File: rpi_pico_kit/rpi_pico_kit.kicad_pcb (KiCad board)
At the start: 2 copper layers, 99.1 x 99.1 mm, 242 parts, among them J1 DC Jack 5.5x2.1mm, J10 OLED Display SSD1306, J11 Conn_01x04_Male, J12 Conn_01x04_Male, J13 AudioJack-CUI-SJ-3523-SMT, J14 AudioJack-CUI-SJ-3523-SMT, J2 USB_B, J3 Conn_01x03_Male, J4 DB15_Female_HighDensity_Mount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, J5 HDMI_A, J6 Conn_01x08_Male, J7 Conn_01x08_Male, J8 Conn_01x08_Male, J9 Micro_SD_Card_Det, Q1 DMN63D8L-7, Q2 DMN63D8L-7, Q3 DMN63D8L-7, Q4 DMN63D8L-7, Q5 DMN63D8L-7, Q6 DMN63D8L-7, Q7 DMN63D8L-7, SW1 SW_Push, SW10 SW_Push, SW2 RotaryEncoder_Switch, SW3 SW_Push, SW4 SW_Push, SW5 SW_Push, SW6 SW_Push, SW7 SW_Push, SW8 SW_Push, SW9 SW_Push, U1 RPi Pico, U10 74LVC2G34GV, U11 PCM5101A, U2 NCP1117-3.3_SOT223, U3 RP2040, U4 W25Q16JVSSIQ, U5 74HC14, U6 74HC14, U7 MCP23S08-xSO, U8 AT24CS32, U9 NCP115-3.3_SOT23-5, Y1 12MHz

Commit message: pcb changes
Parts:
- moved C22 246.1 mm to (174.4, 100.7)
- moved C23 246.1 mm to (160.9, 115.3)
- moved Q3 246.1 mm to (160.9, 111.6)
- moved R25 246.1 mm to (160.7, 122.0)
- moved R26 246.1 mm to (170.6, 113.8)
- moved R27 246.1 mm to (183.9, 103.7)
- moved R28 246.1 mm to (188.7, 100.3)
- moved R29 246.1 mm to (179.1, 106.6)
- moved R32 246.1 mm to (175.4, 112.6)
- moved R35 246.1 mm to (180.1, 109.6)
- moved R36 246.1 mm to (165.4, 121.3)
- moved R37 246.1 mm to (165.6, 118.3)
- moved R38 246.1 mm to (182.8, 97.3)
- moved R41 246.1 mm to (160.8, 118.3)
- moved R42 246.1 mm to (174.3, 106.7)
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
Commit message: pcb changes
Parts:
- moved U7 208.5 mm to (48.6, 185.9)
- moved C1 205.3 mm to (-30.2, 171.8)
- moved C11 205.3 mm to (-25.4, 171.8)
- moved C12 205.3 mm to (-30.2, 174.8)
- moved C14 205.3 mm to (-28.8, 168.8)
- moved C6 205.3 mm to (-23.9, 168.8)
- moved R10 205.3 mm to (-38.5, 186.3)
- moved R12 205.3 mm to (-19.2, 169.1)
- moved R13 205.3 mm to (-19.2, 166.2)
- moved R15 205.3 mm to (-38.5, 189.2)
- moved R17 205.3 mm to (-25.5, 174.7)
- moved R18 205.3 mm to (-29.0, 177.8)
- moved TP4 205.3 mm to (-39.4, 192.2)
- moved C10 205.3 mm to (-38.6, 180.3)
- moved C15 205.3 mm to (-20.4, 163.2)
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
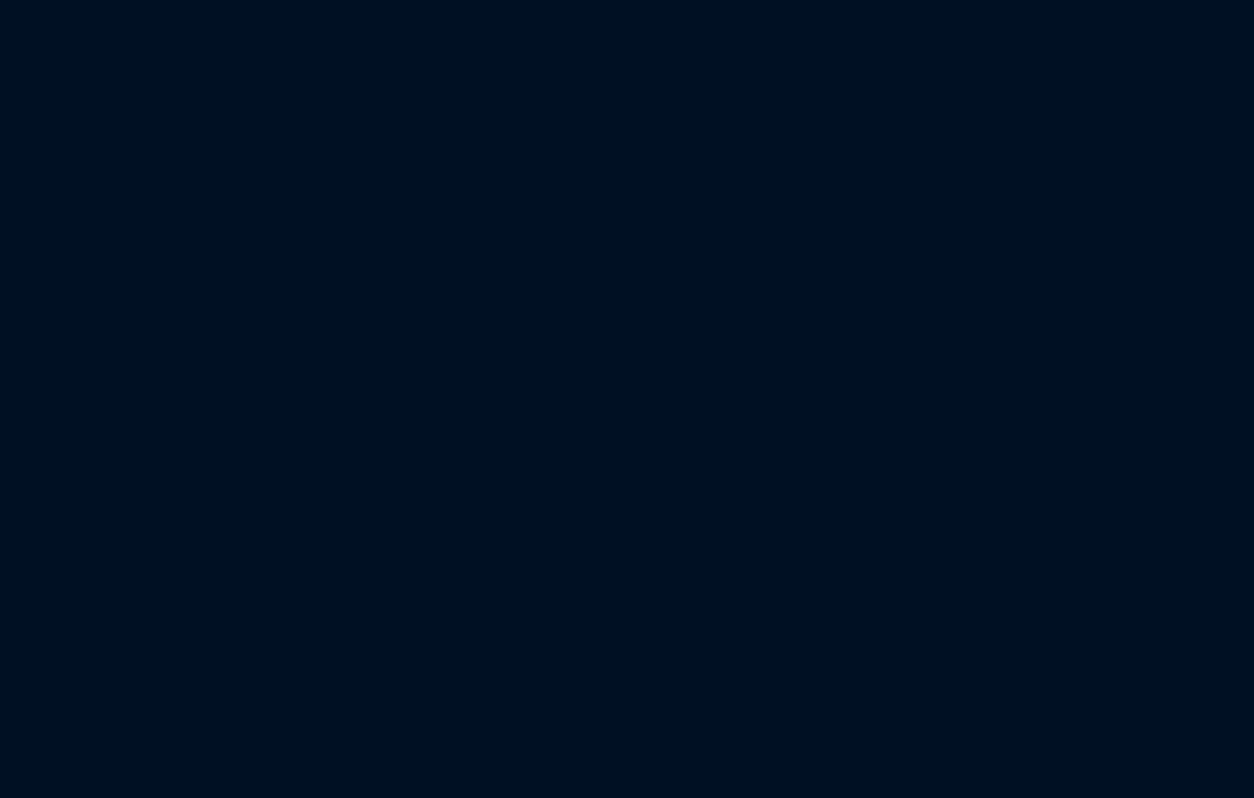
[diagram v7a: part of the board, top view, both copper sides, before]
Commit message: added footprints for resistor arrays
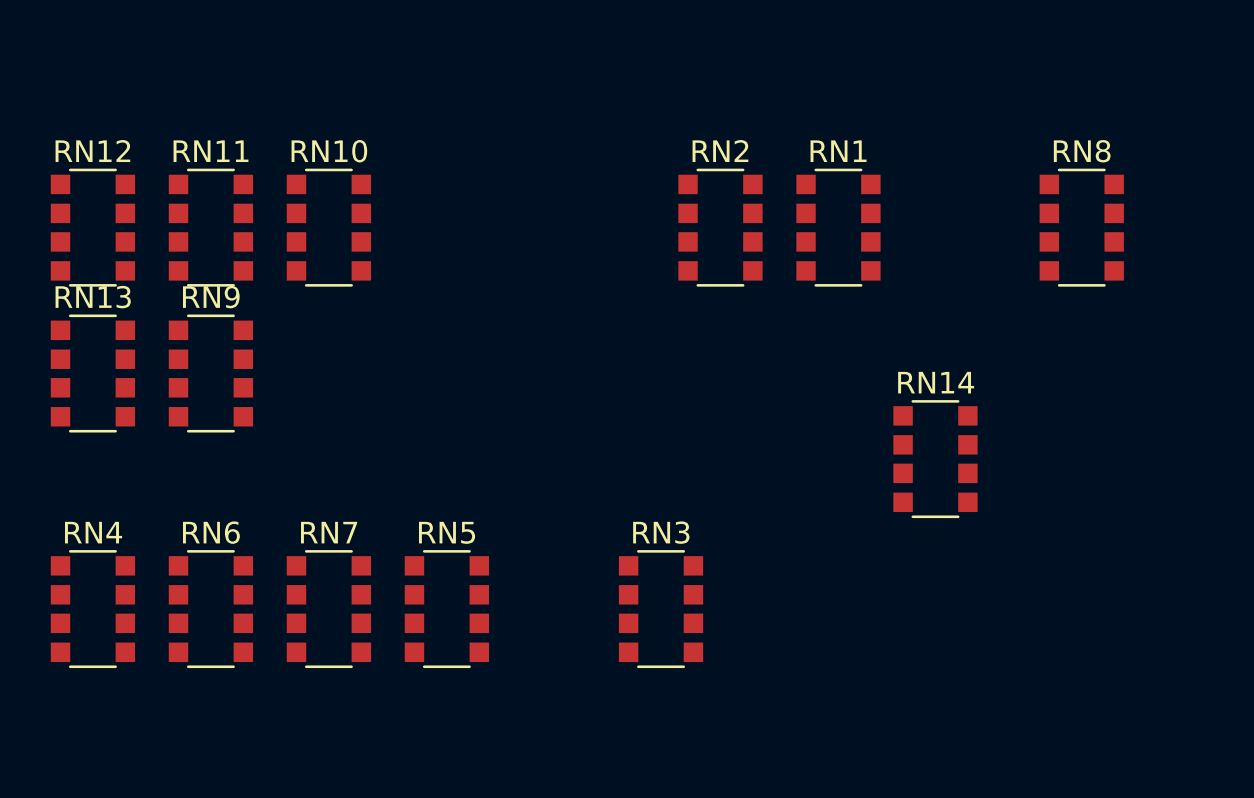
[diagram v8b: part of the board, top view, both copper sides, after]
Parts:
- added RN1: 270R, Resistor_SMD:R_Array_Convex_4x1206, F.Cu at (-98.4, 47.0)
- added RN10: 1k, Resistor_SMD:R_Array_Convex_4x1206, F.Cu at (-122.0, 47.0)
- added RN11: 10k, Resistor_SMD:R_Array_Convex_4x1206, F.Cu at (-127.5, 47.0)
- added RN12: 1k, Resistor_SMD:R_Array_Convex_4x1206, F.Cu at (-132.9, 47.0)
- added RN13: 2k, Resistor_SMD:R_Array_Convex_4x1206, F.Cu at (-132.9, 53.7)
- added RN14: 1k, Resistor_SMD:R_Array_Convex_4x1206, F.Cu at (-93.9, 57.7)
- added RN2: 270R, Resistor_SMD:R_Array_Convex_4x1206, F.Cu at (-103.9, 47.0)
- added RN3: 1k, Resistor_SMD:R_Array_Convex_4x1206, F.Cu at (-106.6, 64.6)
- added RN4: 1k, Resistor_SMD:R_Array_Convex_4x1206, F.Cu at (-132.9, 64.6)
- added RN5: 1k, Resistor_SMD:R_Array_Convex_4x1206, F.Cu at (-116.5, 64.6)
- added RN6: 1k, Resistor_SMD:R_Array_Convex_4x1206, F.Cu at (-127.5, 64.6)
- added RN7: 1k, Resistor_SMD:R_Array_Convex_4x1206, F.Cu at (-122.0, 64.6)
- added RN8: 4.7k, Resistor_SMD:R_Array_Convex_4x1206, F.Cu at (-87.2, 47.0)
- added RN9: 1k, Resistor_SMD:R_Array_Convex_4x1206, F.Cu at (-127.5, 53.7)
- J4: value DB15_Female_HighDensity_MountingHoles -> DB15_Female
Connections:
- R46 pad 1: Net-(R45-Pad2) -> Net-(RN13A-R1.2)
- R47 pad 1: Net-(R45-Pad2) -> Net-(RN13A-R1.2)
- R47 pad 2: Net-(R47-Pad2) -> Net-(RN13B-R2.2)
- R49 pad 1: Net-(R47-Pad2) -> Net-(RN13B-R2.2)
- R49 pad 2: Net-(R49-Pad2) -> Net-(RN13C-R3.2)
- R51 pad 1: Net-(R49-Pad2) -> Net-(RN13C-R3.2)
- SW3 pad 2: Net-(R41-Pad2) -> Net-(RN12A-R1.2)
- SW4 pad 2: Net-(R42-Pad2) -> Net-(RN12B-R2.2)
- SW5 pad 2: Net-(R43-Pad2) -> Net-(RN12C-R3.2)
- SW6 pad 2: Net-(R44-Pad2) -> Net-(RN12D-R4.2)
- TP3 pad 1: Net-(R9-Pad2) -> Net-(RN14A-R1.2)
- TP4 pad 1: Net-(R10-Pad2) -> Net-(RN14B-R2.2)
- U1 pad 1: Net-(U1-GPIO0) -> Net-(RN3B-R2.2)
- U1 pad 2: Net-(U1-GPIO1) -> Net-(RN3D-R4.2)
- U3 pad 2: Net-(U3-GPIO0) -> Net-(RN14A-R1.1)
- U3 pad 3: Net-(U3-GPIO1) -> Net-(RN14B-R2.1)
- U3 pad 4: Net-(U3-GPIO2) -> Net-(RN14C-R3.1)
- U3 pad 5: Net-(U3-GPIO3) -> Net-(RN14D-R4.1)
- U6 pad 1: Net-(R41-Pad2) -> Net-(RN12A-R1.2)
- U6 pad 2: Net-(R52-Pad1) -> Net-(RN13D-R4.1)
- U6 pad 3: Net-(R42-Pad2) -> Net-(RN12B-R2.2)
- U6 pad 4: Net-(R50-Pad1) -> Net-(RN13C-R3.1)
- U6 pad 5: Net-(R43-Pad2) -> Net-(RN12C-R3.2)
- U6 pad 6: Net-(R48-Pad1) -> Net-(RN13B-R2.1)
- U6 pad 8: Net-(R45-Pad1) -> Net-(RN13A-R1.1)
- U6 pad 9: Net-(R44-Pad2) -> Net-(RN12D-R4.2)
